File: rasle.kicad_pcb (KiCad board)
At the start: 2 copper layers, 65 x 56 mm, 69 parts, among them J1 Power, J10 BUTTON4, J11 BUTTON_PWR, J12 External relay, J14 Conn_01x02_Male, J15 Conn_01x02_Male, J2 FAN, J3 LED1, J4 WS2812, J5 LED2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

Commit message: Added manufacturing files
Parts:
- added J13: Reset disable, Pin_Headers:Pin_Header_Straight_1x02, F.Cu at (246.3, 145.2)
- moved C10 2.34 mm to (249.5, 144.5), turned to 270 degrees
- moved J11 0.80 mm to (260.4, 114.5)
- moved R13 0.71 mm to (251.4, 104.5)
- moved R14 0.71 mm to (251.4, 108.0)
- moved C7 0.71 mm to (254.6, 106.0)
- moved C8 0.70 mm to (254.6, 111.1)
- moved J9 0.67 mm to (253.5, 103.4)
- moved J10 0.63 mm to (253.4, 109.0)
- moved L2 0.51 mm to (209.8, 116.3)
- moved L1 0.45 mm to (209.9, 107.2)
- moved L4 0.39 mm to (209.8, 114.6)
- moved L3 0.33 mm to (209.9, 105.5)
- moved J8 0.28 mm to (260.4, 109.0)
- moved J7 0.27 mm to (260.4, 103.4)
- moved C4 0.24 mm to (210.3, 111.7)
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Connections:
- C10 pad 1: /GPIO4(GCLK) -> /RESET_ATMEGA
- R18 pad 1: /GPIO4(GCLK) -> /RESET_ATMEGA
- U1 pad 29: /GPIO4(GCLK) -> /RESET_ATMEGA
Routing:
- net /GPIO4(GCLK): track 0.00 -> 84.3 mm, vias 0 -> 1
- net /RESET_ATMEGA: track 0.00 -> 33.7 mm, vias 0 -> 1
- net +3V3: track 98.6 -> 124.1 mm
- net GND: track 33.2 -> 37.3 mm, vias 12 -> 33
- net /PWM1: track 26.0 -> 29.1 mm
- net /BCLK: track 28.7 -> 31.3 mm
- net /WS2812_DATA: track 51.3 -> 53.8 mm
- net /PWM2: track 54.7 -> 52.8 mm
- net /GPIO24(GEN5): track 53.4 -> 55.0 mm
- net /GPIO15(RXD0): track 66.4 -> 64.9 mm
- net /FAN: track 36.5 -> 37.9 mm
- net /GPIO14(TXD0): track 68.5 -> 69.8 mm
- net /GPIO9(SPI0_MISO): track 58.0 -> 59.2 mm
- net /BUTTON3: track 13.1 -> 11.9 mm
- net /GPIO11(SPI0_SCK): track 51.5 -> 52.6 mm
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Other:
- rule trace_min: 0.1524 -> 0.2

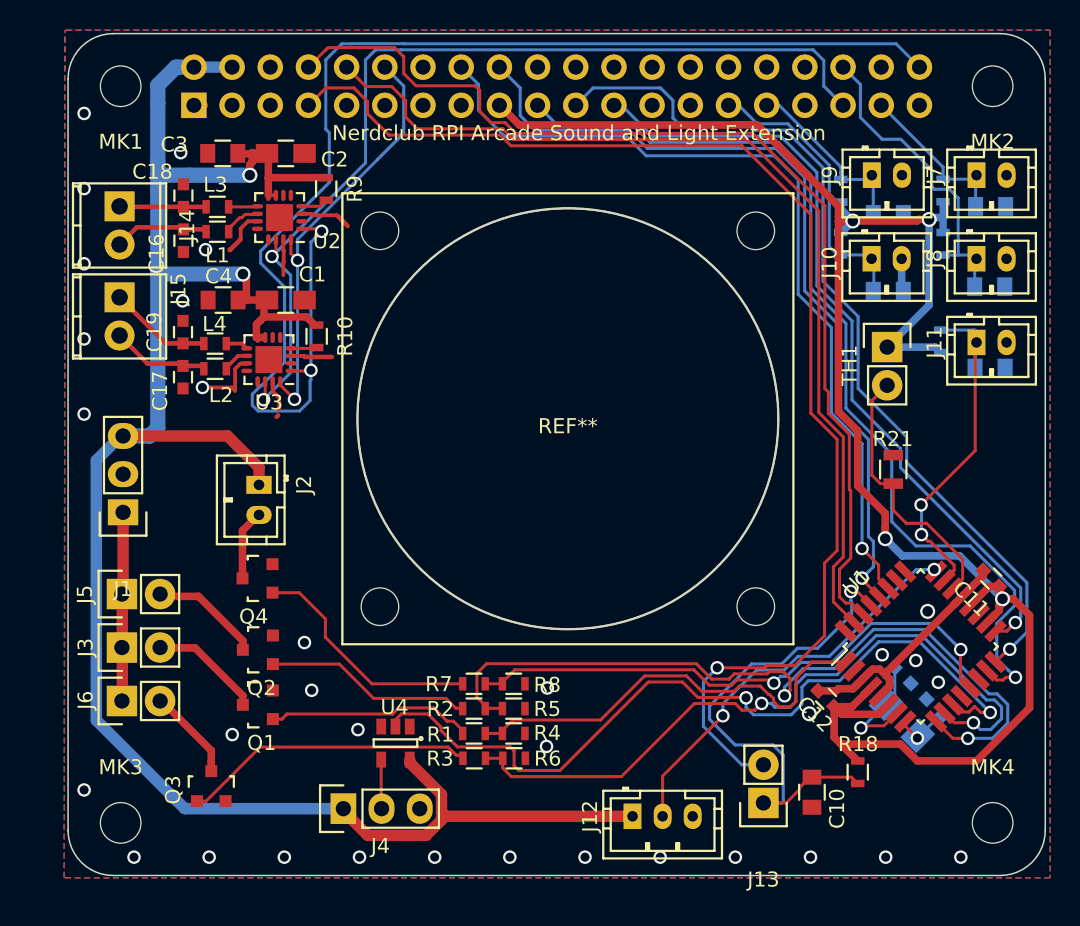
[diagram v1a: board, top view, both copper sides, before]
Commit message: Added EEPROM for HAT compatability
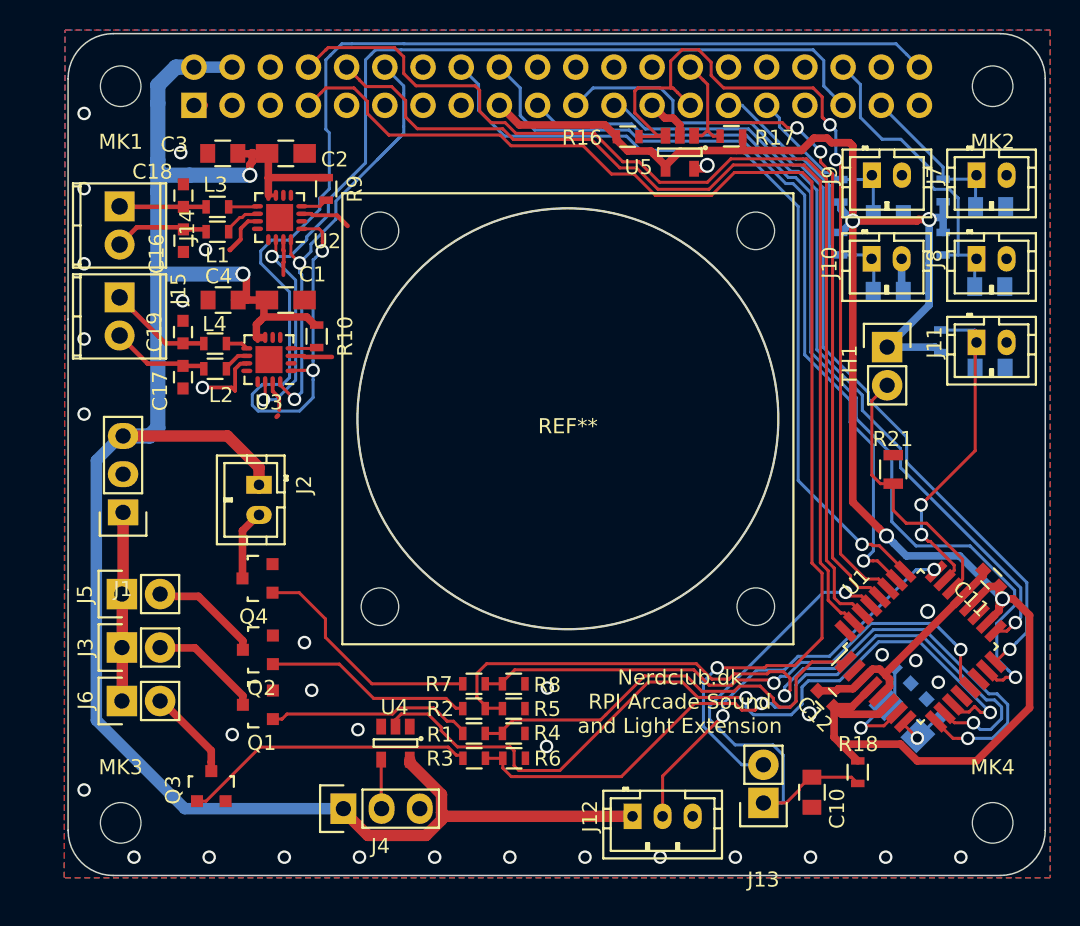
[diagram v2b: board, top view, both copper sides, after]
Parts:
- added R16: R, Resistors_SMD:R_0603, F.Cu at (237.2, 100.9)
- added R17: R, Resistors_SMD:R_0603, F.Cu at (244.1, 100.8)
- added U5: 24AA02-OT, TO_SOT_Packages_SMD:SOT-23-5, F.Cu at (240.7, 101.9)
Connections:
- U1 pad 25: Net-(U1-Pad25) -> /GPIO23(GEN4)
- U1 pad 26: Net-(U1-Pad26) -> /GPIO24(GEN5)
- U1 pad 27: /GPIO23(GEN4) -> /ID_SD
- U1 pad 28: /GPIO24(GEN5) -> /ID_SC
- U2 pad 17: (no net) -> Net-(U2-Pad17)
- U3 pad 17: (no net) -> Net-(U3-Pad17)
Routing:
- net /ID_SD: track 0.00 -> 59.2 mm, vias 0 -> 2
- net /ID_SC: track 0.00 -> 46.8 mm, vias 0 -> 2
- net +3V3: track 124.1 -> 128.7 mm
- net GND: track 37.3 -> 41.5 mm, vias 33 -> 34
- net /GPIO15(RXD0): track 64.9 -> 67.1 mm
- net /GPIO14(TXD0): track 69.8 -> 71.8 mm
- net /DIN: track 85.8 -> 87.7 mm
- net /GPIO4(GCLK): track 84.3 -> 86.0 mm
- net /GPIO19(SPI1_MISO): track 63.5 -> 64.9 mm
- net /GPIO23(GEN4): track 56.2 -> 55.1 mm
- net /RESET_ATMEGA: track 33.7 -> 32.7 mm
- net /GPIO24(GEN5): track 55.0 -> 54.1 mm
- net /BUTTON4: track 19.2 -> 18.5 mm
- net /GPIO9(SPI0_MISO): track 59.2 -> 58.4 mm
- net /GPIO11(SPI0_SCK): track 52.6 -> 51.9 mm
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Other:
- board text added: "Nerdclub.dk RPI Arcade Sound and Light Extension"
- board text removed: "Nerdclub RPI Arcade Sound and Light Extension"

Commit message: Added RTC chip for timekeeping
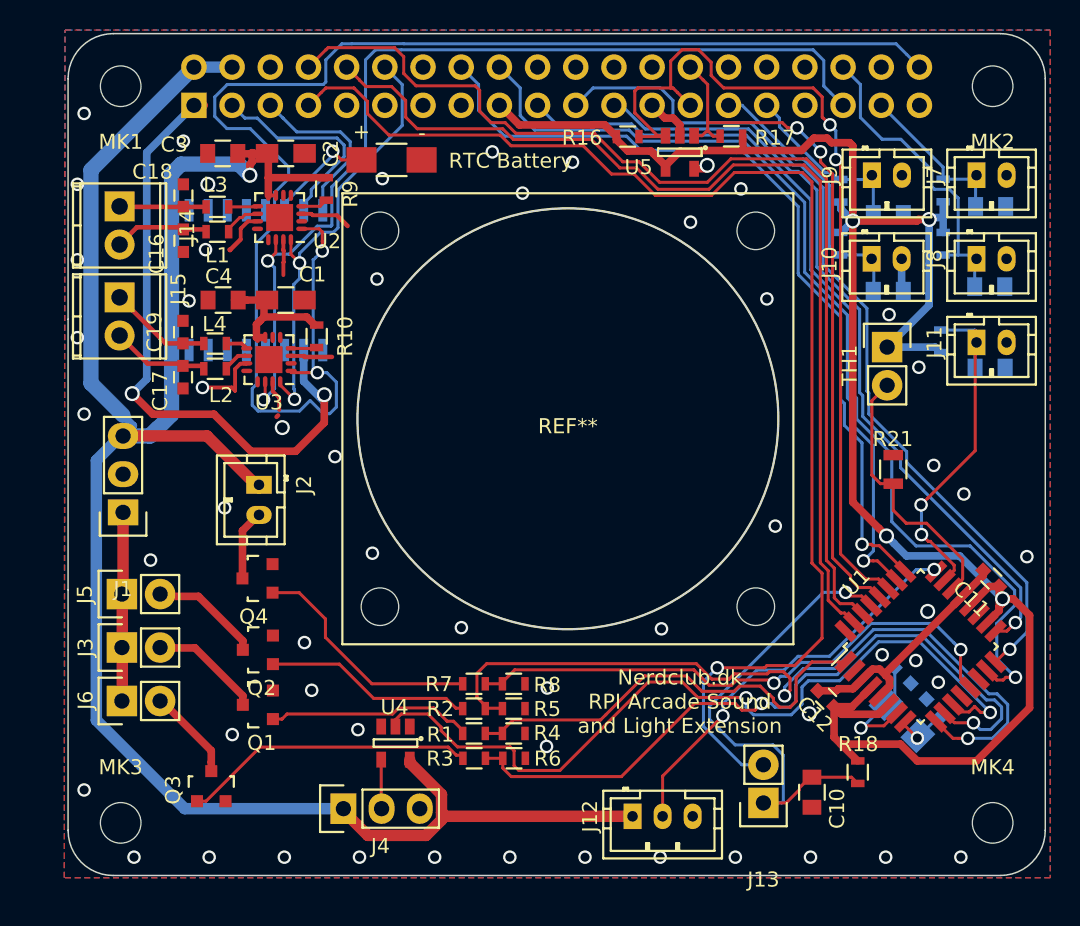
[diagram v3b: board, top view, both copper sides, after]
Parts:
- added J16: Conn_01x02_Male, Resistors_SMD:R_1206_HandSoldering, F.Cu at (221.5, 102.4)
- added U6: DS3231M, Housings_SOIC:SOIC-16_7.5x10.3mm_Pitch1.27mm, B.Cu at (212.5, 110.4)
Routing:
- net +3V3: track 128.7 -> 171.4 mm, vias 4 -> 6
- net /GPIO2(SDA1): track 0.00 -> 14.0 mm
- net +5V: track 138.9 -> 151.4 mm, vias 2 -> 1
- net /GPIO3(SCL1): track 0.00 -> 11.6 mm
- net /DIN: track 87.7 -> 97.2 mm
- net +BATT: track 0.00 -> 7.41 mm, vias 0 -> 1
- net /BCLK: track 31.7 -> 29.5 mm
- net /GPIO19(SPI1_MISO): track 64.9 -> 64.3 mm
- net GND: vias 34 -> 56
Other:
- board text added: "+"
- board text added: "-"
- board text added: "RTC Battery"

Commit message: Removed RTC chip as it is not necessary
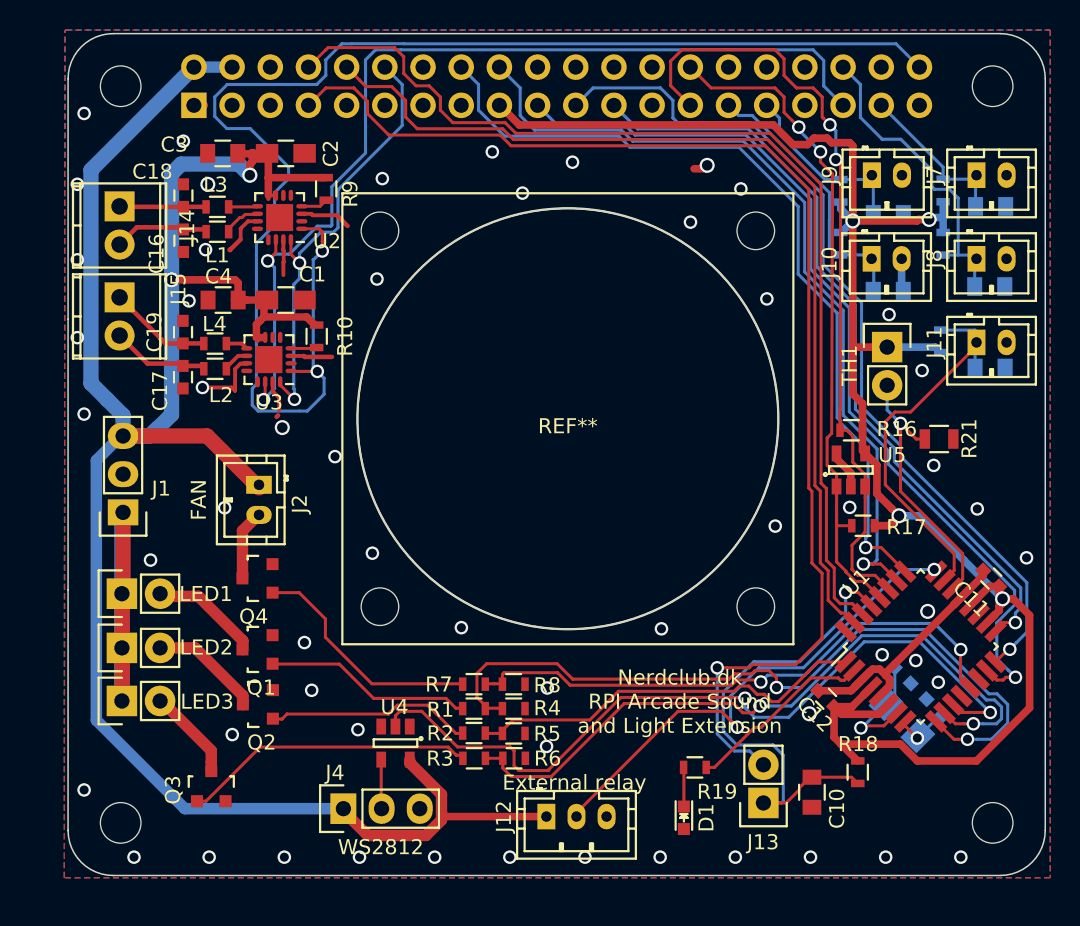
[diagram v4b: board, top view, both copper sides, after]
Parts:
- removed J16: Conn_01x02_Male, Resistors_SMD:R_1206_HandSoldering
- removed U6: DS3231M, Housings_SOIC:SOIC-16_7.5x10.3mm_Pitch1.27mm
- added D1: LED, LEDs:LED-0603, F.Cu at (241.0, 146.2)
- added R19: 220R, Resistors_SMD:R_0603, F.Cu at (241.7, 142.8)
- C1, C2: value CP -> 10uF
- C10, C11, C12, C3, C4, C5, C6, C7, C8, C9: value C -> 100nF
- C14, C15: value C -> 22pF
- C16, C17, C18, C19: value C -> 220nF
- R1, R2, R3, R7: value R -> 0R
- R11, R12, R13, R14, R15, R18, R4, R5, R6, R8: value R -> 10k
- R16, R17: value R -> 4k7
- moved R17 27.3 mm to (252.9, 126.7)
- moved R16 24.5 mm to (252.1, 120.4), turned to 180 degrees
- moved U5 24.0 mm to (252.1, 123.0), turned to 90 degrees
- moved J12 5.73 mm to (231.8, 146.1)
- moved Q1 3.68 mm to (212.6, 135.0)
- moved R21 3.66 mm to (257.9, 121.0), turned to 0 degrees
- moved Q2 3.63 mm to (212.6, 138.6)
- moved LED1 3.58 mm to (203.6, 131.3)
- moved LED2 3.58 mm to (203.6, 134.9)
- moved R1 1.65 mm to (227.0, 138.9)
- moved R4 1.65 mm to (229.6, 138.9)
- moved R5 1.65 mm to (229.6, 140.6)
- moved R2 1.63 mm to (227.0, 140.5)
- renumbered J3 to LED1, J5 to LED2, J6 to LED3
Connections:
- U1 pad 1: /PWM1 -> /PWM2
- U1 pad 9: /PWM2 -> /PWM1
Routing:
- net +3V3: track 171.4 -> 119.8 mm, vias 6 -> 4
- net /PWM2: track 52.8 -> 26.9 mm, vias 2 -> 0
- net /PWM1: track 29.1 -> 51.3 mm, vias 0 -> 2
- net /GPIO2(SDA1): track 14.0 -> 0.00 mm
- net Net-(R19-Pad1): track 0.00 -> 12.6 mm
- net +12V: track 12.5 -> 25.1 mm
- net /GPIO3(SCL1): track 11.6 -> 0.00 mm
- net +BATT: track 7.41 -> 0.00 mm, vias 1 -> 0
- net /ID_SD: track 59.2 -> 52.0 mm
- net /POWER: track 27.1 -> 33.7 mm
- net /DIN: track 97.2 -> 94.1 mm
- net /GPIO4(GCLK): track 86.0 -> 83.3 mm
- net Net-(D1-Pad1): track 0.00 -> 2.61 mm
- net /GPIO10(SPI0_MOSI): track 63.5 -> 61.4 mm
- net /GPIO14(TXD0): track 71.8 -> 69.8 mm
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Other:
- board text removed: "+"
- board text removed: "-"
- board text removed: "RTC Battery"

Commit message: Minor touchup / beautifying of routing
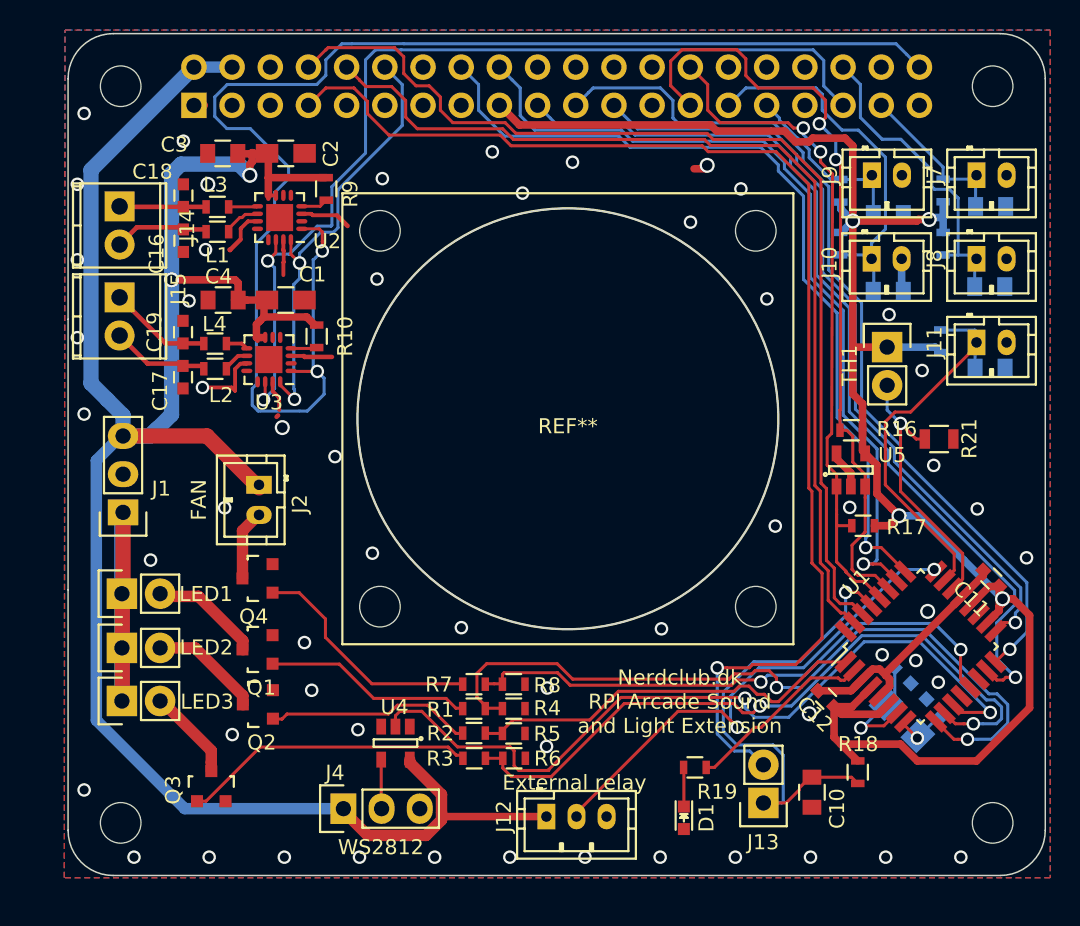
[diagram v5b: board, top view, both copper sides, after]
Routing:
- net /BUTTON4: track 18.2 -> 25.1 mm
- net /GPIO10(SPI0_MOSI): track 61.4 -> 62.3 mm
- net /GPIO11(SPI0_SCK): track 51.6 -> 52.5 mm
- net /GPIO9(SPI0_MISO): track 58.2 -> 59.0 mm
- net /GPIO23(GEN4): track 55.2 -> 56.1 mm
- net /GPIO24(GEN5): track 54.6 -> 55.3 mm
- net /ID_SC: track 45.3 -> 45.9 mm

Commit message: Connected atmega to all buttons, so it can listen to the same button events as RPI
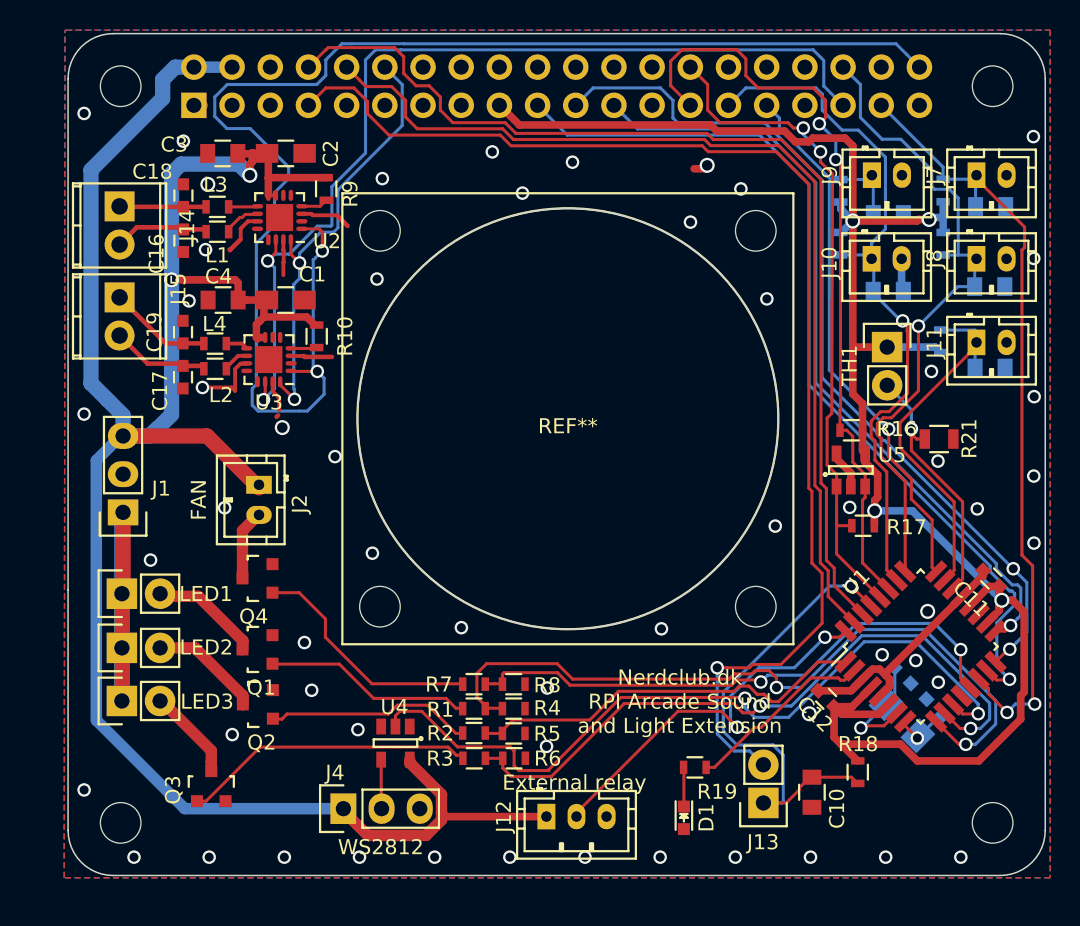
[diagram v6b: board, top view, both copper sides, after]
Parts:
- LED1: value LED1 -> PWM
- LED2: value LED2 -> PWM
- LED3: value LED3 -> PWM
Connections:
- U1 pad 14: Net-(U1-Pad14) -> /BUTTON1
- U1 pad 24: /POWER -> /BUTTON3
- U1 pad 25: /GPIO23(GEN4) -> /BUTTON2
- U1 pad 26: /GPIO24(GEN5) -> /BUTTON4
- U1 pad 32: Net-(U1-Pad32) -> /POWER
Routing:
- net /GPIO23(GEN4): track 56.1 -> 0.00 mm, vias 1 -> 0
- net /GPIO24(GEN5): track 55.3 -> 0.00 mm, vias 1 -> 0
- net /BUTTON1: track 10.6 -> 52.6 mm, vias 0 -> 2
- net /BUTTON3: track 11.8 -> 40.9 mm, vias 0 -> 1
- net /BUTTON2: track 21.2 -> 44.6 mm, vias 0 -> 1
- net /BUTTON4: track 25.1 -> 47.3 mm, vias 0 -> 1
- net /POWER: track 33.7 -> 25.9 mm
- net /BTN_PWR: track 25.9 -> 24.5 mm
- net /ID_SD: track 52.4 -> 51.1 mm
- net /PWM3: track 46.6 -> 45.4 mm
- net /WS2812_DATA: track 52.3 -> 51.2 mm
- net /PWM1: track 51.3 -> 50.2 mm
- net +5V: track 150.7 -> 151.5 mm
- net /GPIO10(SPI0_MOSI): track 62.3 -> 61.5 mm
- net Net-(R21-Pad1): track 17.9 -> 17.2 mm
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
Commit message: PCB manufacturing
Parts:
- J12: footprint Connectors_JST_PH:Connectors_JST_B3B-PH-K -> Pin_Headers:Pin_Header_Straight_1x03
- moved J12 0.40 mm to (231.8, 145.7), turned to 90 degrees
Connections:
- U2 pad 17: Net-(U2-Pad17) -> GND
- U3 pad 17: Net-(U3-Pad17) -> GND
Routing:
- net /DIN: track 94.1 -> 66.4 mm, vias 2 -> 3
- net /GPIO19(SPI1_MISO): track 64.3 -> 66.1 mm
- net +3V3: track 119.3 -> 118.6 mm
- net /GPIO9(SPI0_MISO): track 58.8 -> 58.6 mm, vias 2 -> 1
- net GND: track 41.9 -> 42.0 mm, vias 57 -> 65
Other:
- net class Default: via_dia 0.9 -> 0.6; via_drill 0.6 -> 0.4
- rule via_min_drill: 0.5 -> 0.4
- rule via_min_size: 0.8 -> 0.6
- board text added: "NerdClub.dk"
- board text added: "RPI Arcade Sound and Light Extension"
- board text removed: "Nerdclub.dk RPI Arcade Sound and Light Extension"
